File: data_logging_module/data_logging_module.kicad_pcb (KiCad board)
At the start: 4 copper layers, 80 x 40 mm, 60 parts, among them J1 Conn_01x15, J2 Conn_01x15, J200 10067847-001RLF, U100 TLV62569DBV, U101 HT7533-1, U300 BME280, U301 BME280, U400 PCF8563TS, U5 DS18B20, Y400 32768Hz

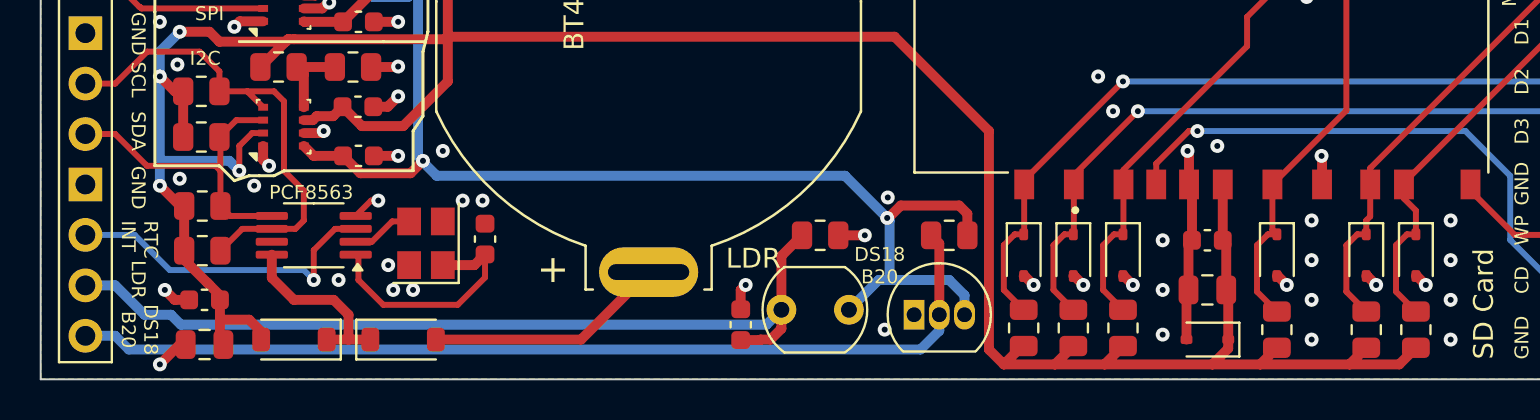
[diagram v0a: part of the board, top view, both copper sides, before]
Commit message: Add decoupling capacitors to analog sensors
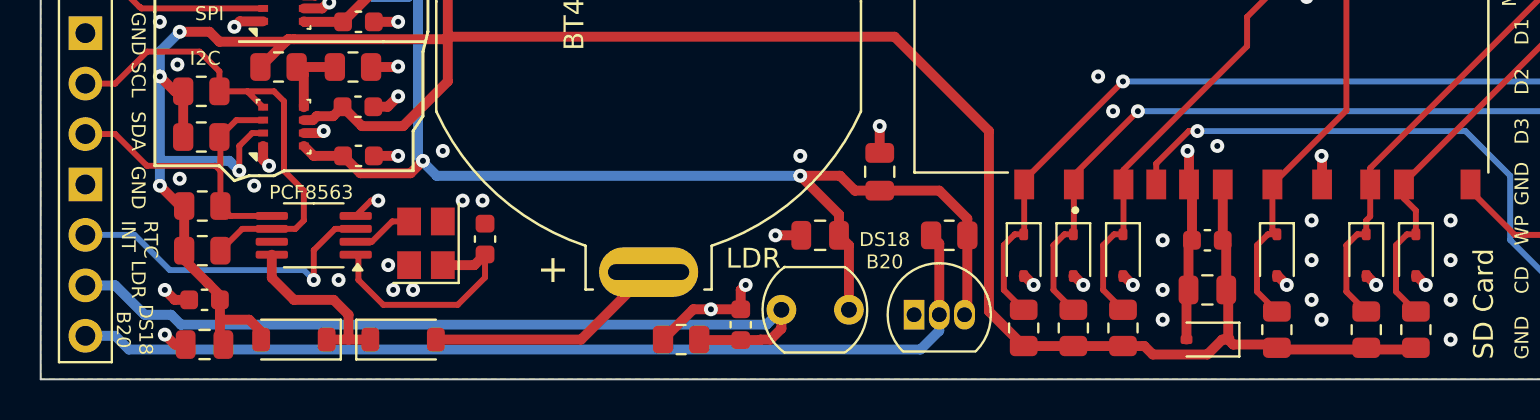
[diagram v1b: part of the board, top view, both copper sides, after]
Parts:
- added C301: 10uF, Capacitor_SMD:C_0805_2012Metric, F.Cu at (111.8, 80.2)
- added C302: 10uF, Capacitor_SMD:C_0805_2012Metric, F.Cu at (114.8, 77.0)
- moved R300 8.75 mm to (104.8, 85.5), turned to 180 degrees
- renumbered C301 to C303, C302 to C304, C303 to C305, C304 to C306
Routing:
- net +3.3V: track 261.3 -> 252.3 mm
- net GND: track 42.5 -> 47.9 mm, vias 77 -> 78
- net LDR: track 43.6 -> 41.5 mm

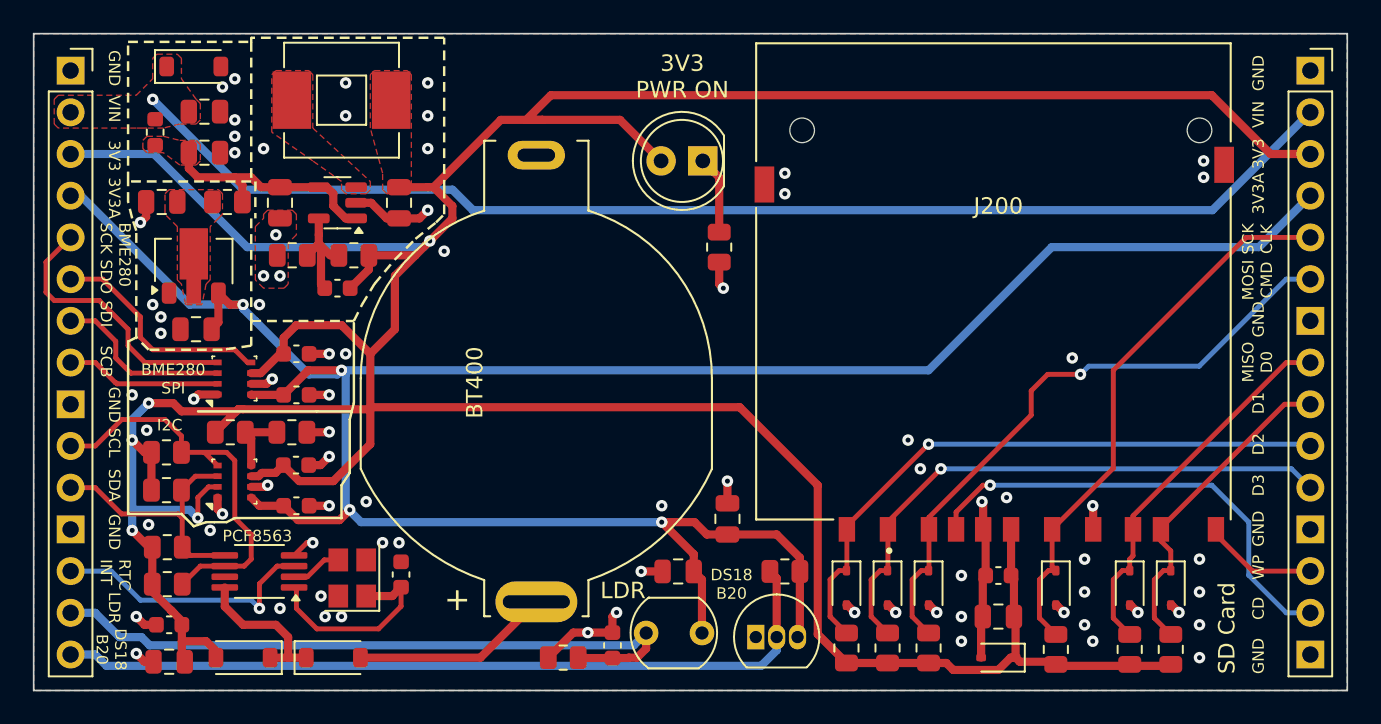
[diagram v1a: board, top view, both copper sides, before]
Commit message: Remove front copper mask
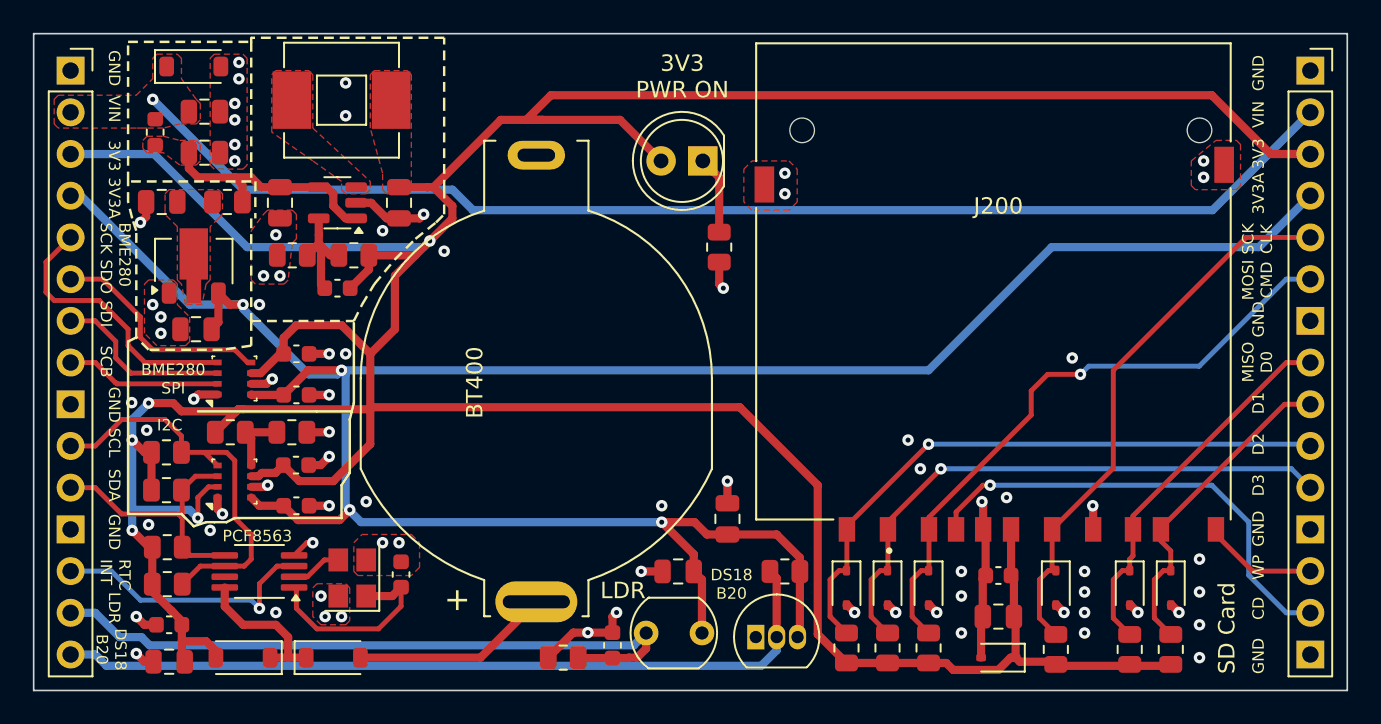
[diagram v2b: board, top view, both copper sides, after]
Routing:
- net GND: track 47.9 -> 47.5 mm, vias 78 -> 76
- removed copper zone on B.Cu, net GND
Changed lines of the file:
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@@
 	)
 	(segment
+		(start 96 58.75)
+		(end 94.75 58.75)
+		(width 0.5)
+		(layer "F.Cu")
+		(net 1)
+	)
+	(segment
 		(start 105.3625 83.975)
 		(end 106.25 83.975)
@@
 	)
 	(segment
+		(start 82.525 69.475)
+		(end 83.7 69.475)
+		(width 0.5)
+		(layer "F.Cu")
+		(net 1)
+	)
+	(segment
 		(start 122.05 82.3)
 		(end 122.5 82.75)
@@
 	)
 	(segment
-		(start 82.525 69.475)
-		(end 83.7 69.475)
-		(width 0.5)
-		(layer "F.Cu")
-		(net 1)
-	)
-	(segment
 		(start 137.025 76.275)
 		(end 137 76.25)
@@
 	)
 	(segment
-		(start 94.75 58.75)
-		(end 96 58.75)
-		(width 0.5)
-		(layer "F.Cu")
-		(net 1)
-	)
-	(segment
 		(start 89.1375 78.5)
 		(end 88.3625 79.275)
@@
 	)
 	(segment
+		(start 96.25 58.5)
+		(end 96 58.75)
+		(width 0.5)
+		(layer "F.Cu")
+		(net 1)
+	)
+	(segment
 		(start 89.975 73.775)
 		(end 90.5 73.25)
@@
 	)
 	(segment
-		(start 96 58.75)
-		(end 96.5 58.25)
-		(width 0.5)
-		(layer "F.Cu")
-		(net 1)
-	)
-	(segment
 		(start 79.35 58.65)
 		(end 79 59)
@@
 	)
 	(via
-		(at 86.5 54.5)
-		(size 0.7)
-		(drill 0.3)
-		(layers "F.Cu" "B.Cu")
-		(free yes)
-		(net 1)
-	)
-	(via
 		(at 90.5 67)
 		(size 0.7)
@@
 	)
 	(via
-		(at 96.5 52.5)
-		(size 0.7)
-		(drill 0.3)
-		(layers "F.Cu" "B.Cu")
-		(free yes)
-		(net 1)
-	)
-	(via
 		(at 87.030331 68.530331)
 		(size 0.7)
@@
 	)
 	(via
-		(at 78.5 69.5)
+		(at 78.469669 69.969669)
 		(size 0.7)
 		(drill 0.3)
@@
 	)
 	(via
-		(at 137 84.5)
-		(size 0.7)
-		(drill 0.3)
-		(layers "F.Cu" "B.Cu")
-		(free yes)
-		(net 1)
-	)
-	(via
-		(at 96.5 54.5)
+		(at 136.5 84)
 		(size 0.7)
 		(drill 0.3)
@@
 	)
 	(via
-		(at 136.5 83.5)
+		(at 136.5 82.75)
 		(size 0.7)
 		(drill 0.3)
@@
 	)
 	(via
-		(at 129 84.5)
+		(at 129 84)
 		(size 0.7)
 		(drill 0.3)
@@
 	)
 	(via
-		(at 129 83)
+		(at 129 80.25)
 		(size 0.7)
 		(drill 0.3)
@@
 	)
 	(via
-		(at 96.5 50.5)
-		(size 0.7)
-		(drill 0.3)
-		(layers "F.Cu" "B.Cu")
-		(free yes)
-		(net 1)
-	)
-	(via
 		(at 90.5 76.25)
 		(size 0.7)
@@
 	)
 	(via
-		(at 84 50.75)
+		(at 85 50.25)
 		(size 0.7)
 		(drill 0.3)
@@
 	)
 	(via
-		(at 84.75 53.75)
+		(at 84.75 54.25)
 		(size 0.7)
 		(drill 0.3)
@@
 	)
 	(via
-		(at 129 80.5)
+		(at 129 81.75)
 		(size 0.7)
 		(drill 0.3)
@@
 	)
 	(via
-		(at 84.75 50.25)
+		(at 85 49.25)
 		(size 0.7)
 		(drill 0.3)
@@
 	)
 	(via
-		(at 136.5 79.5)
+		(at 136.5 80.25)
 		(size 0.7)
 		(drill 0.3)
@@
 	)
 	(via
+		(at 93.75 59.5)
+		(size 0.7)
+		(drill 0.3)
+		(layers "F.Cu" "B.Cu")
+		(free yes)
+		(net 1)
+	)
+	(via
 		(at 78.75 83)
 		(size 0.7)
@@
 	)
 	(via
-		(at 96.5 58.25)
+		(at 96.25 58.5)
 		(size 0.7)
 		(drill 0.3)
@@
 	)
 	(via
+		(at 84.75 51.75)
+		(size 0.7)
+		(drill 0.3)
+		(layers "F.Cu" "B.Cu")
+		(free yes)
+		(net 1)
+	)
+	(via
 		(at 143.5 83.5)
 		(size 0.7)
@@
 	)
 	(via
-		(at 87.5 82.5)
+		(at 87.25 82.75)
 		(size 0.7)
 		(drill 0.3)
@@
 	)
 	(via
-		(at 84.75 54.75)
+		(at 84.75 55.25)
 		(size 0.7)
 		(drill 0.3)
@@
 	)
 	(zone
+		(net 1)
+		(net_name "GND")
+		(layer "F.Cu")
+		(hatch edge 0.5)
+		(priority 10)
+		(connect_pads yes
+			(clearance 0.5)
+		)
+		(min_thickness 0.25)
+		(filled_areas_thickness no)
+		(fill yes
+			(thermal_gap 0.5)
+			(thermal_bridge_width 0.5)
+		)
+		(polygon
+			(pts
+				(xy 143 55.25) (xy 144.5 54) (xy 145.75 54) (xy 146 54.25) (xy 146 56.75) (xy 145.75 57) (xy 143.25 57)
+				(xy 143 56.75)
+			)
+		)
+	)
+	(zone
+		(net 1)
+		(net_name "GND")
+		(layer "F.Cu")
+		(hatch edge 0.5)
+		(priority 8)
+		(connect_pads yes
+			(clearance 0.5)
+		)
+		(min_thickness 0.25)
+		(filled_areas_thickness no)
+		(fill yes
+			(thermal_gap 0.5)
+			(thermal_bridge_width 0.5)
+		)
+		(polygon
+			(pts
+				(xy 89.5 81.25) (xy 89.75 81) (xy 91.5 81) (xy 91.75 81.25) (xy 91.75 83.25) (xy 91.5 83.5) (xy 90 83.5)
+				(xy 89.5 83)
+			)
+		)
+	)
+	(zone
 		(net 5)
 		(net_name "+5V")
@@
 		(polygon
 			(pts
-				(xy 86.5 58.5) (xy 86.75 58.25) (xy 88.25 58.25) (xy 88.5 58.5) (xy 88.5 59.75) (xy 88 60.25) (xy 88 62.75)
-				(xy 87.75 63) (xy 86.5 63) (xy 86 62.5) (xy 86 59.25) (xy 86.5 58.75)
+				(xy 86.5 58.5) (xy 86.75 58.25) (xy 88.25 58.25) (xy 88.5 58.5) (xy 88.5 60) (xy 88.25 60.25) (xy 88 62.5)
+				(xy 87.75 62.75) (xy 86 62.75) (xy 85.75 62.5) (xy 85.75 59.5)
 			)
 		)
@@
 	)
 	(zone
+		(net 1)
+		(net_name "GND")
+		(layer "F.Cu")
+		(hatch edge 0.5)
+		(priority 1)
+		(connect_pads yes
+			(clearance 0.5)
+		)
+		(min_thickness 0.25)
+		(filled_areas_thickness no)
+		(fill yes
+			(thermal_gap 0.5)
+			(thermal_bridge_width 0.5)
+		)
+		(polygon
+			(pts
+				(xy 83.25 49) (xy 83.5 48.75) (xy 85.25 48.75) (xy 85.5 49) (xy 85.5 55.5) (xy 85.25 55.75) (xy 83.5 55.75)
+				(xy 83.25 55.5)
+			)
+		)
+	)
+	(zone
+		(net 1)
+		(net_name "GND")
+		(layer "F.Cu")
+		(hatch edge 0.5)
+		(priority 7)
+		(connect_pads yes
+			(clearance 0.5)
+		)
+		(min_thickness 0.25)
+		(filled_areas_thickness no)
+		(fill yes
+			(thermal_gap 0.5)
+			(thermal_bridge_width 0.5)
+		)
+		(polygon
+			(pts
+				(xy 92 78.5) (xy 92.5 78) (xy 95.5 78) (xy 96 78.5) (xy 96 80) (xy 95.5 80.5) (xy 92.25 80.5) (xy 92 80.25)
+			)
+		)
+	)
+	(zone
+		(net 1)
+		(net_name "GND")
+		(layer "F.Cu")
+		(hatch edge 0.5)
+		(priority 9)
+		(connect_pads yes
+			(clearance 0.5)
+		)
+		(min_thickness 0.25)
+		(filled_areas_thickness no)
+		(fill yes
+			(thermal_gap 0.5)
+			(thermal_bridge_width 0.5)
+		)
+		(polygon
+			(pts
+				(xy 79.25 62.75) (xy 79.5 62.5) (xy 81 62.5) (xy 81.25 62.75) (xy 81.25 64) (xy 82 64.75) (xy 82 66.25)
+				(xy 81.75 66.5) (xy 80 66.5) (xy 79.25 65.75)
+			)
+		)
+	)
+	(zone
+		(net 1)
+		(net_name "GND")
+		(layer "F.Cu")
+		(hatch edge 0.5)
+		(priority 11)
+		(connect_pads yes
+			(clearance 0.5)
+		)
+		(min_thickness 0.25)
+		(filled_areas_thickness no)
+		(fill yes
+			(thermal_gap 0.5)
+			(thermal_bridge_width 0.5)
+		)
+		(polygon
+			(pts
+				(xy 115.75 55.75) (xy 116.25 55.25) (xy 118.5 55.25) (xy 119 55.75) (xy 119 57.75) (xy 118.5 58.25)
+				(xy 116.25 58.25) (xy 115.75 57.75)
+			)
+		)
+	)
+	(zone
 		(net 3)
 		(net_name "+3.3V")
@@
 		(net 1)
 		(net_name "GND")
-		(layers "F.Cu" "In1.Cu" "In2.Cu" "B.Cu")
+		(layers "In1.Cu" "In2.Cu")
 		(hatch edge 0.5)
 		(connect_pads yes
